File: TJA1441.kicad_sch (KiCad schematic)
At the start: 5 parts

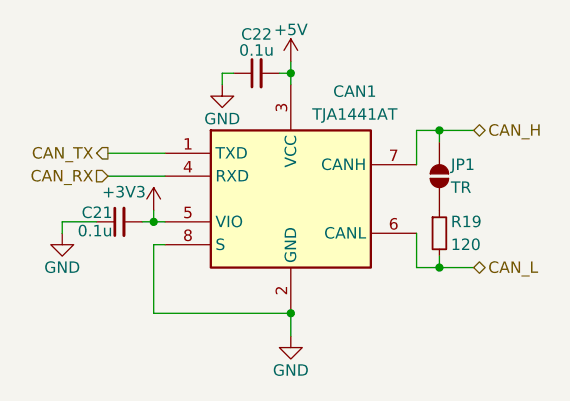
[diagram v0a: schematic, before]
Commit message: 抜けてたフォトカプラの抵抗を追加
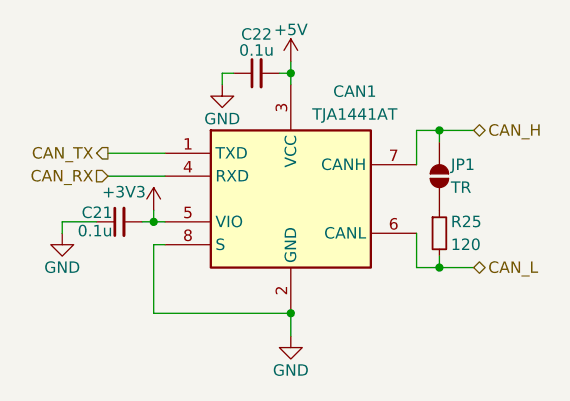
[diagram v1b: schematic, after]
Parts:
- renumbered R19 to R25
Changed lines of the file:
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@@
 		(on_board yes)
 		(dnp no)
-		(property "Reference" "R19"
+		(property "Reference" "R25"
 			(at 121.92 69.85 0)
 			(effects
@@
 			(project "DRC-PumpDriver2026"
 				(path "/cf42be67-fab3-494c-b2b5-38aff4068810/3a4a56d4-04c8-4cdb-9269-7809d127a6ab"
-					(reference "R19")
+					(reference "R25")
 					(unit 1)
 				)
